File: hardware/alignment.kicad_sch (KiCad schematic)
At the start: 22 parts, among them J202 P3, J203 P2, J205 P6

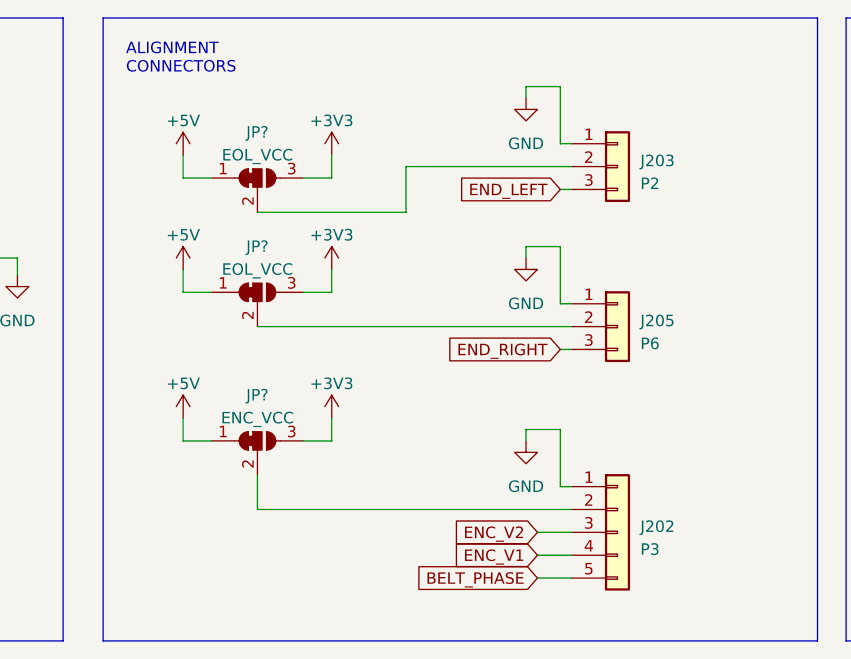
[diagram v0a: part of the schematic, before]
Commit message: work on firmware and swap solenoid banks to match actual pinout
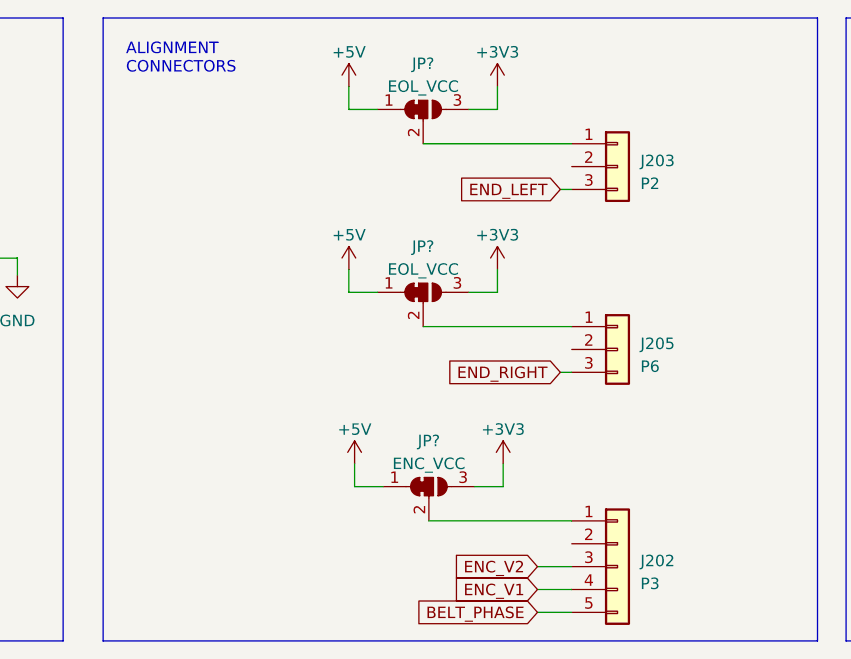
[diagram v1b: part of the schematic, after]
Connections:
- net GND: no longer J202.1 (Pin_1), J203.1 (Pin_1), J205.1 (Pin_1)
- net at JP?.2 (C): now also J203.1 (Pin_1); no longer J203.2 (Pin_2)
- net at JP?.2 (C): now also J205.1 (Pin_1); no longer J205.2 (Pin_2)
- net at JP?.2 (C): now also J202.1 (Pin_1); no longer J202.2 (Pin_2)
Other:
- moved on the sheet: J202, J205, JP?
